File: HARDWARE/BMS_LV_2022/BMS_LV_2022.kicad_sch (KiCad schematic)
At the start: 35 parts, among them J1 USB-C_GCT_USB4145-03-0070-C, J2 Conn_01x12_Male, J4 Battery+, J5 Battery-, J7 FTSH, SW1 SW_Push, U1 STM32L4P5RET6, Y1 Crystal

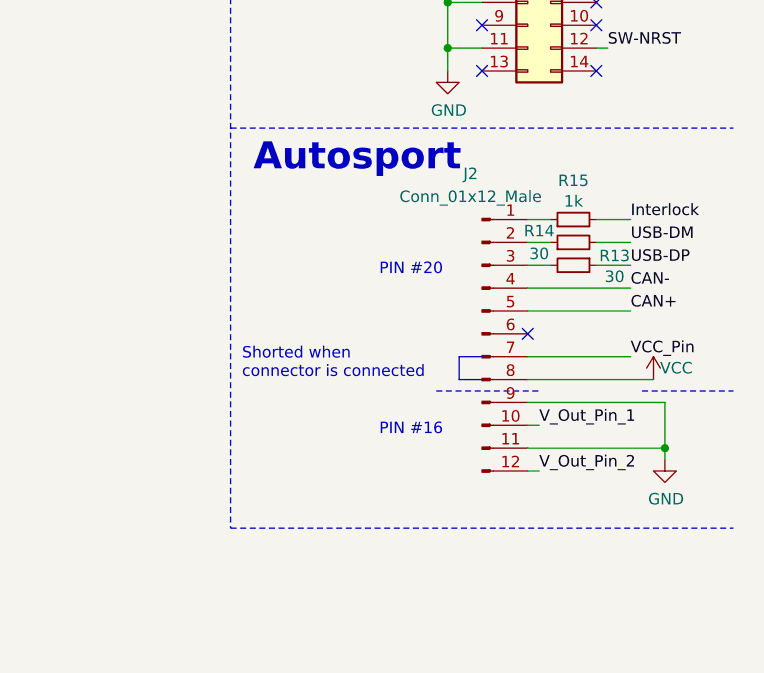
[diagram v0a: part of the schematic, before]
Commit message: Autosport connector scheme updated
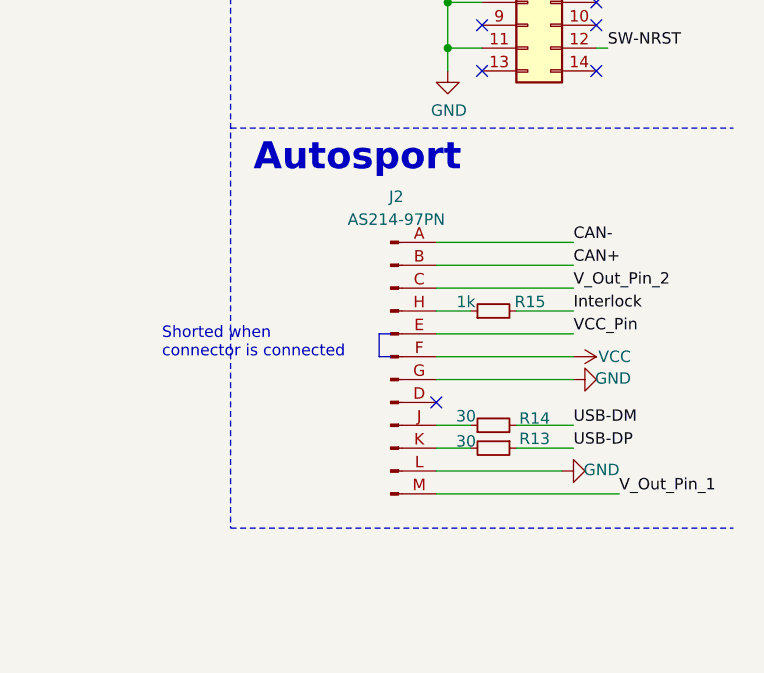
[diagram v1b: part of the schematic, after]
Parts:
- removed J2: Conn_01x12_Male, footprints:AS214-97PN, symbol BMS_LV_2022-rescue:Conn_01x12_Male-Connector
- added J2: AS214-97PN, footprints:AS214-97PN, symbol as214-97pn:Conn_01x12_Male-Connector
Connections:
- net CAN+: now also J2.B
- net CAN-: now also J2.A
- net GND: now also J2.G, J2.L
- net VCC: now also J2.F
- net VCC_Pin: now also J2.E
- net V_Out_Pin_1: now also J2.M
- net V_Out_Pin_2: now also J2.C
- net at R15.1: now also J2.H
- net at R14.1: now also J2.J
- net at R13.2: now also J2.K
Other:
- note removed: "PIN #16"
- note removed: "PIN #20"
- moved on the sheet: R13, R14, R15
